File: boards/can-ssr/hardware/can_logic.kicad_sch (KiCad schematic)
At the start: 31 parts, among them J1 CAN IN, J2 CAN OUT, J3 ICSP, J4 UART, SW1 ADDR, U1 R-78E5.0-1.0, U2 MCP2562FD-E/P, U3 PIC18F47Q84-I/PT, Y1 16MHz

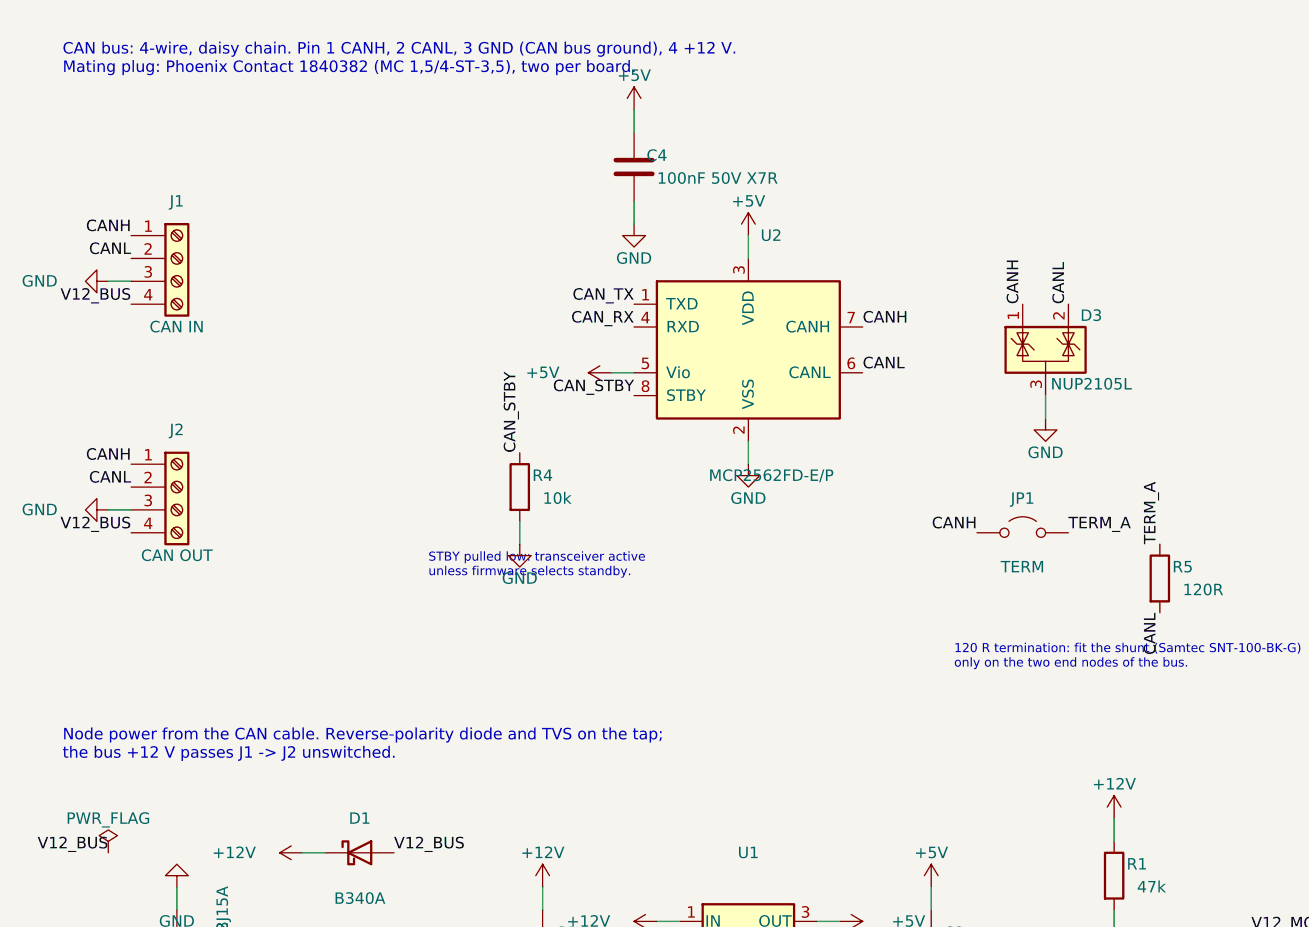
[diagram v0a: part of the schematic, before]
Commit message: can-ssr: stack interface rework; MCDN double-level CAN header; Ethernet parts
can-ssr (checker clean: ERC, DRC, schematic parity):
- M4 standoff holes 4.5 mm in from each corner (91 x 91 mm), new
  Thl_Mechanical:MountingHole_4.3mm_M4_Standoff7mm (4.3 mm courtyard, both
  sides); copper keep-outs around the load-side holes
- Load bolts moved inward (S+ 18, S- 36, L- 63, L+ 82 mm) with bars, mask
  openings, return bar, pours and labels
- Top-right corner reworked for the MH2 standoff (LED column, R50/C44,
  local reroutes); scoped DRC rule for MH2 beside U40
- CAN IN + CAN OUT -> one Phoenix MCDN 1,5/4-G1-3,5 P26 THR (1953732) at the
  stack CAN position (pin 1 at y 15.5 mm); schematic J1 is Conn_02x04,
  J2 removed; SW1/D2 moved; affected nets rejoined locally
- One-off rework scripts kept in hardware/stack_rework/

Library and tools:
- Footprint generator for the MCDN header (own drawing from Phoenix's
  dimensions); vendor STEP is local-only (SamacSys licence)
- tools/miniroute.py: small two-layer grid router for local rework

Requirements: stack CAN position fixed at pin 1 = 15.5 mm; holes at 4.5 mm;
can-controller Ethernet parts JD0-0004NL jack and HI1206P121R-10 bead (W6100).

Co-Authored-By: Claude Opus 5.5 <noreply@anthropic.com>
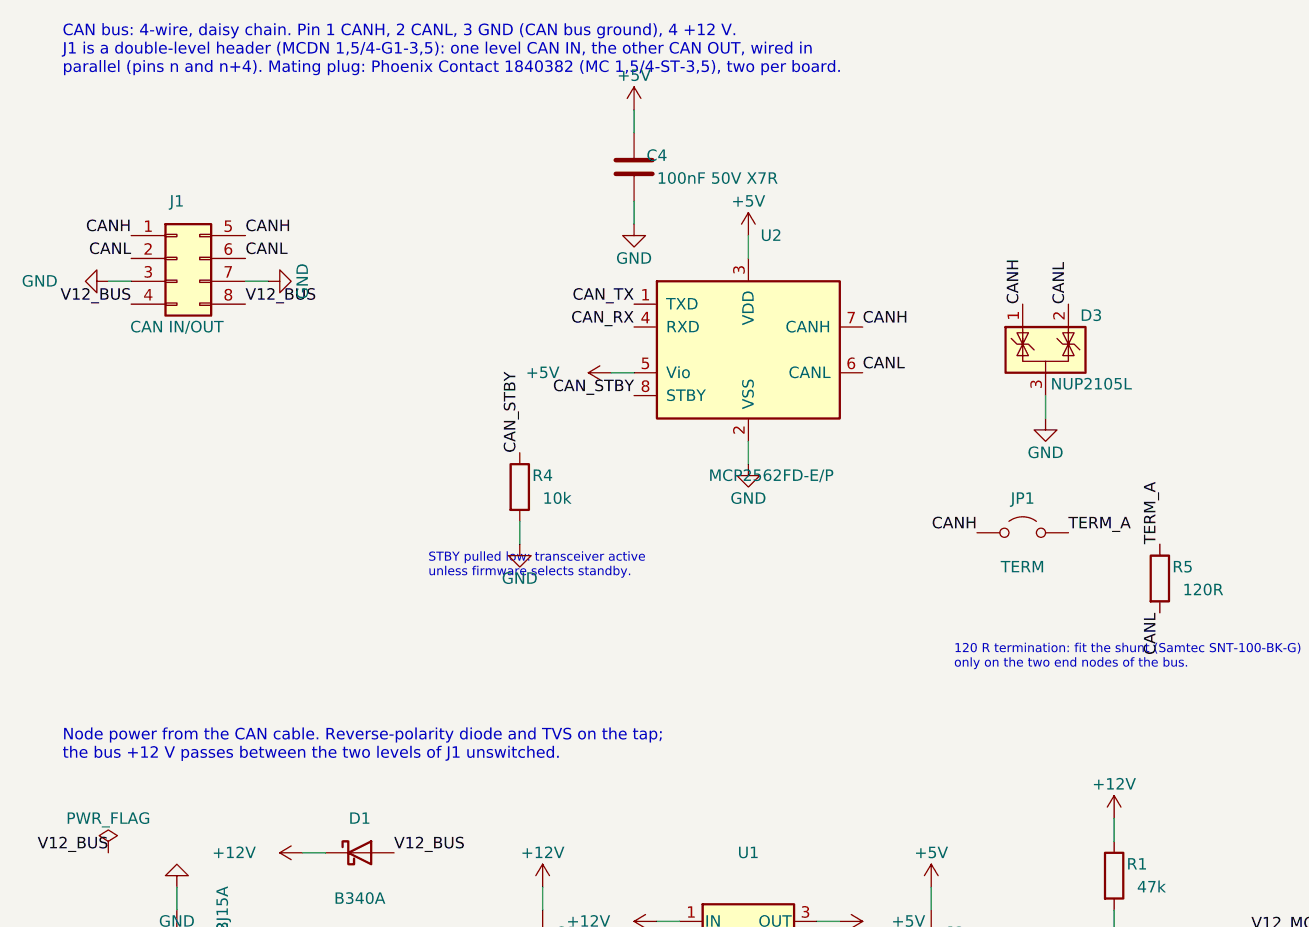
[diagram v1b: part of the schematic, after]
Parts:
- removed J2: CAN OUT, Connector_Phoenix_MC:PhoenixContact_MC_1,5_4-G-3.5_1x04_P3.50mm_Horizontal, symbol Connector:Screw_Terminal_01x04
- J1: value CAN IN -> CAN IN/OUT; footprint Connector_Phoenix_MC:PhoenixContact_MC_1,5_4-G-3.5_1x04_P3.50mm_Horizontal -> Thl_Connector:PhoenixContact_MCDN_1,5_4-G1-3,5_2x04_P3.5mm_Horizontal; symbol Connector:Screw_Terminal_01x04 -> Connector_Generic:Conn_02x04_Top_Bottom; MPN 1844236 -> 1953732
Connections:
- net CANH: now also J1.5 (Pin_5)
- net CANL: now also J1.6 (Pin_6)
- net GND: now also J1.7 (Pin_7)
- net V12_BUS: now also J1.8 (Pin_8)
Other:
- note added: "CAN bus: 4-wire, daisy chain. Pin 1 CANH, 2 CANL, 3 GND (CAN bus ground), 4 +12 V. J1 is a double-level header (MCDN 1,5/4-G1-3,5): one level CAN IN, the other CAN OUT, wired in parallel (pins n and n+4). Mating plug: Phoenix Contact 1840382 (MC 1,5/4-ST-3,5), two per board."
- note added: "Node power from the CAN cable. Reverse-polarity diode and TVS on the tap; the bus +12 V passes between the two levels of J1 unswitched."
- note removed: "CAN bus: 4-wire, daisy chain. Pin 1 CANH, 2 CANL, 3 GND (CAN bus ground), 4 +12 V. Mating plug: Phoenix Contact 1840382 (MC 1,5/4-ST-3,5), two per board."
- note removed: "Node power from the CAN cable. Reverse-polarity diode and TVS on the tap; the bus +12 V passes J1 -> J2 unswitched."
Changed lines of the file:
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@@
 		(rev "A")
 	)
-	(text "CAN bus: 4-wire, daisy chain. Pin 1 CANH, 2 CANL, 3 GND (CAN bus ground), 4 +12 V.\nMating plug: Phoenix Contact 1840382 (MC 1,5/4-ST-3,5), two per board."
+	(text "CAN bus: 4-wire, daisy chain. Pin 1 CANH, 2 CANL, 3 GND (CAN bus ground), 4 +12 V.\nJ1 is a double-level header (MCDN 1,5/4-G1-3,5): one level CAN IN, the other CAN OUT, wired in\nparallel (pins n and n+4). Mating plug: Phoenix Contact 1840382 (MC 1,5/4-ST-3,5), two per board."
 		(exclude_from_sim no)
 		(at 25.4 30.48 0)
@@
 	)
 	(symbol
-		(lib_id "Connector:Screw_Terminal_01x04")
+		(lib_id "Connector_Generic:Conn_02x04_Top_Bottom")
 		(at 38.1 50.8 0)
 		(unit 1)
@@
 			)
 		)
-		(property "Value" "CAN IN"
+		(property "Value" "CAN IN/OUT"
 			(at 38.1 58.42 0)
 			(effects
@@
 			)
 		)
-		(property "Footprint" "Connector_Phoenix_MC:PhoenixContact_MC_1,5_4-G-3.5_1x04_P3.50mm_Horizontal"
+		(property "Footprint" "Thl_Connector:PhoenixContact_MCDN_1,5_4-G1-3,5_2x04_P3.5mm_Horizontal"
 			(at 38.1 50.8 0)
 			(hide yes)
@@
 			)
 		)
-		(property "MPN" "1844236"
+		(property "MPN" "1953732"
 			(at 38.1 50.8 0)
 			(hide yes)
@@
 		)
 		(pin "4"
+		)
+		(pin "5"
+		)
+		(pin "6"
+		)
+		(pin "7"
+		)
+		(pin "8"
 		)
 		(instances
@@
 		)
 	)
-	(symbol
-		(lib_id "Connector:Screw_Terminal_01x04")
-		(at 38.1 76.2 0)
-		(unit 1)
-		(exclude_from_sim no)
-		(in_bom yes)
-		(on_board yes)
-		(dnp no)
-		(property "Reference" "J2"
-			(at 38.1 69.85 0)
-			(effects
-				(font
-					(size 1.27 1.27)
-				)
-			)
-		)
-		(property "Value" "CAN OUT"
-			(at 38.1 83.82 0)
-			(effects
-				(font
-					(size 1.27 1.27)
-				)
-			)
-		)
-		(property "Footprint" "Connector_Phoenix_MC:PhoenixContact_MC_1,5_4-G-3.5_1x04_P3.50mm_Horizontal"
-			(at 38.1 76.2 0)
-			(hide yes)
-			(effects
-				(font
-					(size 1.27 1.27)
-				)
-			)
-		)
-		(property "Datasheet" ""
-			(at 38.1 76.2 0)
-			(hide yes)
-			(effects
-				(font
-					(size 1.27 1.27)
-				)
-			)
-		)
-		(property "Description" ""
-			(at 38.1 76.2 0)
-			(hide yes)
-			(effects
-				(font
-					(size 1.27 1.27)
-				)
-			)
-		)
-		(property "Manufacturer" "Phoenix Contact"
-			(at 38.1 76.2 0)
-			(hide yes)
-			(effects
-				(font
-					(size 1.27 1.27)
-				)
-			)
-		)
-		(property "MPN" "1844236"
-			(at 38.1 76.2 0)
-			(hide yes)
-			(effects
-				(font
-					(size 1.27 1.27)
-				)
-			)
-		)
-		(pin "1"
-		)
-		(pin "2"
-		)
-		(pin "3"
-		)
-		(pin "4"
-		)
-		(instances
-			(project "can-ssr"
-				(path "/09b96810-cbdb-496a-83a0-e49ecf8d36fe/c853aef6-a14e-49c9-8f13-7d5eddc0f3e9"
-					(reference "J2")
-					(unit 1)
-				)
-			)
-		)
-	)
 	(label "CANH"
-		(at 33.02 73.66 180)
-		(effects
-			(font
-				(size 1.27 1.27)
-			)
-			(justify right bottom)
+		(at 45.72 48.26 0)
+		(effects
+			(font
+				(size 1.27 1.27)
+			)
+			(justify left bottom)
 		)
 	)
 	(label "CANL"
-		(at 33.02 76.2 180)
-		(effects
-			(font
-				(size 1.27 1.27)
-			)
-			(justify right bottom)
+		(at 45.72 50.8 0)
+		(effects
+			(font
+				(size 1.27 1.27)
+			)
+			(justify left bottom)
 		)
 	)
 	(wire
 		(pts
-			(xy 33.02 78.74) (xy 30.48 78.74)
+			(xy 45.72 53.34) (xy 48.26 53.34)
 		)
 		(stroke
@@
 	(symbol
 		(lib_id "power:GND")
-		(at 30.48 78.74 270)
+		(at 48.26 53.34 90)
 		(unit 1)
 		(exclude_from_sim no)
@@
 		(dnp no)
 		(property "Reference" "#PWR02"
-			(at 30.48 76.2 0)
+			(at 48.26 50.8 0)
 			(hide yes)
 			(effects
@@
 		)
 		(property "Value" "GND"
-			(at 22.86 78.74 270)
+			(at 52.07 53.34 0)
 			(effects
 				(font
@@
 		)
 		(property "Footprint" ""
-			(at 30.48 78.74 0)
-			(hide yes)
-			(effects
-				(font
-					(size 1.27 1.27)
-				)
-			)
-		)
-		(property "Datasheet" ""
-			(at 30.48 78.74 0)
-			(hide yes)
-			(effects
-				(font
-					(size 1.27 1.27)
-				)
-			)
-		)
-		(property "Description" ""
-			(at 30.48 78.74 0)
+			(at 48.26 53.34 0)
+			(hide yes)
+			(effects
+				(font
+					(size 1.27 1.27)
+				)
+			)
+		)
+		(property "Datasheet" ""
+			(at 48.26 53.34 0)
+			(hide yes)
+			(effects
+				(font
+					(size 1.27 1.27)
+				)
+			)
+		)
+		(property "Description" ""
+			(at 48.26 53.34 0)
 			(hide yes)
 			(effects
@@
 	)
 	(label "V12_BUS"
-		(at 33.02 81.28 180)
-		(effects
-			(font
-				(size 1.27 1.27)
-			)
-			(justify right bottom)
+		(at 45.72 55.88 0)
+		(effects
+			(font
+				(size 1.27 1.27)
+			)
+			(justify left bottom)
 		)
 	)
@@
 		)
 	)
-	(text "Node power from the CAN cable. Reverse-polarity diode and TVS on the tap;\nthe bus +12 V passes J1 -> J2 unswitched."
+	(text "Node power from the CAN cable. Reverse-polarity diode and TVS on the tap;\nthe bus +12 V passes between the two levels of J1 unswitched."
 		(exclude_from_sim no)
 		(at 25.4 106.68 0)

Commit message: Move core, can-card, io-card, serial-card, can-ssr, probe-helper to rev B
Rev A went to PCBWay and is tagged revA. Rev B replaces parts the Mouser
BOM check flagged (obsolete, end of life, not recommended for new designs,
or not orderable) and swaps out-of-stock passives and diodes for in-stock
equivalents. Field-only changes, same footprints, no layout change; the
reference boards (can-controller, pic-module) get the same part numbers.
The rev A order lists (DigiKey, Mouser) carry the same substitutions; the
Mouser list leaves out the T821 box headers (bought from DigiKey).

docs/rev-b-changes.md lists every change and the rev B to-dos (MAX7219 is
obsolete and must be replaced). transfer/mouser-revA.xlsx (Mouser BOM
check) consumed.

Co-Authored-By: Claude Opus 5.5 <noreply@anthropic.com>
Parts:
- C1, C2, C7: MPN GRM31CR71E106KA12L -> CL31B106KAHNNNE; Manufacturer Murata -> Samsung Electro-Mechanics
- C3, C4, C5, C6: MPN GRM21BR71H104KA01L -> C0805C104K5RACTU; Manufacturer Murata -> KEMET
- C8, C9: MPN GRM2165C1H270JA01D -> C0805C270J5GACTU; Manufacturer Murata -> KEMET
- D4: MPN LTST-C150GKT -> LTST-C150KGKT
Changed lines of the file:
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@@
 		(title "CAN SSR: CAN, power, MCU")
 		(date "2026-10-04")
-		(rev "A")
+		(rev "B")
 	)
 	(text "CAN bus: 4-wire, daisy chain. Pin 1 CANH, 2 CANL, 3 GND (CAN bus ground), 4 +12 V.\nJ1 is a double-level header (MCDN 1,5/4-G1-3,5): one level CAN IN, the other CAN OUT, wired in\nparallel (pins n and n+4). Mating plug: Phoenix Contact 1840382 (MC 1,5/4-ST-3,5), two per board."
@@
 			)
 		)
-		(property "Manufacturer" "Murata"
+		(property "Manufacturer" "KEMET"
 			(at 88.9 40.64 0)
 			(hide yes)
@@
 			)
 		)
-		(property "MPN" "GRM21BR71H104KA01L"
+		(property "MPN" "C0805C104K5RACTU"
 			(at 88.9 40.64 0)
 			(hide yes)
@@
 			)
 		)
-		(property "Manufacturer" "Murata"
+		(property "Manufacturer" "Samsung Electro-Mechanics"
 			(at 78.74 127 0)
 			(hide yes)
@@
 			)
 		)
-		(property "MPN" "GRM31CR71E106KA12L"
+		(property "MPN" "CL31B106KAHNNNE"
 			(at 78.74 127 0)
 			(hide yes)
@@
 			)
 		)
-		(property "Manufacturer" "Murata"
+		(property "Manufacturer" "Samsung Electro-Mechanics"
 			(at 121.92 127 0)
 			(hide yes)
@@
 			)
 		)
-		(property "MPN" "GRM31CR71E106KA12L"
+		(property "MPN" "CL31B106KAHNNNE"
 			(at 121.92 127 0)
 			(hide yes)
@@
 			)
 		)
-		(property "Manufacturer" "Murata"
+		(property "Manufacturer" "KEMET"
 			(at 157.48 132.08 0)
 			(hide yes)
@@
 			)
 		)
-		(property "MPN" "GRM21BR71H104KA01L"
+		(property "MPN" "C0805C104K5RACTU"
 			(at 157.48 132.08 0)
 			(hide yes)
@@
 			)
 		)
-		(property "Manufacturer" "Murata"
+		(property "Manufacturer" "KEMET"
 			(at 223.52 60.96 0)
 			(hide yes)
@@
 			)
 		)
-		(property "MPN" "GRM21BR71H104KA01L"
+		(property "MPN" "C0805C104K5RACTU"
 			(at 223.52 60.96 0)
 			(hide yes)
@@
 			)
 		)
-		(property "Manufacturer" "Murata"
+		(property "Manufacturer" "KEMET"
 			(at 246.38 60.96 0)
 			(hide yes)
@@
 			)
 		)
-		(property "MPN" "GRM21BR71H104KA01L"
+		(property "MPN" "C0805C104K5RACTU"
 			(at 246.38 60.96 0)
 			(hide yes)
@@
 			)
 		)
-		(property "Manufacturer" "Murata"
+		(property "Manufacturer" "Samsung Electro-Mechanics"
 			(at 269.24 60.96 0)
 			(hide yes)
@@
 			)
 		)
-		(property "MPN" "GRM31CR71E106KA12L"
+		(property "MPN" "CL31B106KAHNNNE"
 			(at 269.24 60.96 0)
 			(hide yes)
@@
 			)
 		)
-		(property "Manufacturer" "Murata"
+		(property "Manufacturer" "KEMET"
 			(at 187.96 60.96 0)
 			(hide yes)
@@
 			)
 		)
-		(property "MPN" "GRM2165C1H270JA01D"
+		(property "MPN" "C0805C270J5GACTU"
 			(at 187.96 60.96 0)
 			(hide yes)
@@
 			)
 		)
-		(property "Manufacturer" "Murata"
+		(property "Manufacturer" "KEMET"
 			(at 205.74 60.96 0)
 			(hide yes)
@@
 			)
 		)
-		(property "MPN" "GRM2165C1H270JA01D"
+		(property "MPN" "C0805C270J5GACTU"
 			(at 205.74 60.96 0)
 			(hide yes)
@@
 			)
 		)
-		(property "MPN" "LTST-C150GKT"
+		(property "MPN" "LTST-C150KGKT"
 			(at 241.3 180.34 0)
 			(hide yes)

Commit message: Rev B / rev A order: 10 uF CL31B106KAHZW6E, beads BLM31PG391SN1L
Both earlier substitutes (CL31B106KAHNNNE, BLM31KN102SH1L) are on
backorder at Mouser. CL31B106KAHZW6E has the same rating (1.4 mm tall).
The isolated-supply beads need no 1 kOhm: TI's reference uses 330 Ohm;
BLM31PG391SN1L is 390 Ohm @ 100 MHz, 2 A, 50 mOhm. Field-only changes;
order lists regenerated.

Co-Authored-By: Claude Opus 5.5 <noreply@anthropic.com>
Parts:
- C1, C2, C7: MPN CL31B106KAHNNNE -> CL31B106KAHZW6E
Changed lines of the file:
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@@
 			)
 		)
-		(property "MPN" "CL31B106KAHNNNE"
+		(property "MPN" "CL31B106KAHZW6E"
 			(at 78.74 127 0)
 			(hide yes)
@@
 			)
 		)
-		(property "MPN" "CL31B106KAHNNNE"
+		(property "MPN" "CL31B106KAHZW6E"
 			(at 121.92 127 0)
 			(hide yes)
@@
 			)
 		)
-		(property "MPN" "CL31B106KAHNNNE"
+		(property "MPN" "CL31B106KAHZW6E"
 			(at 269.24 60.96 0)
 			(hide yes)

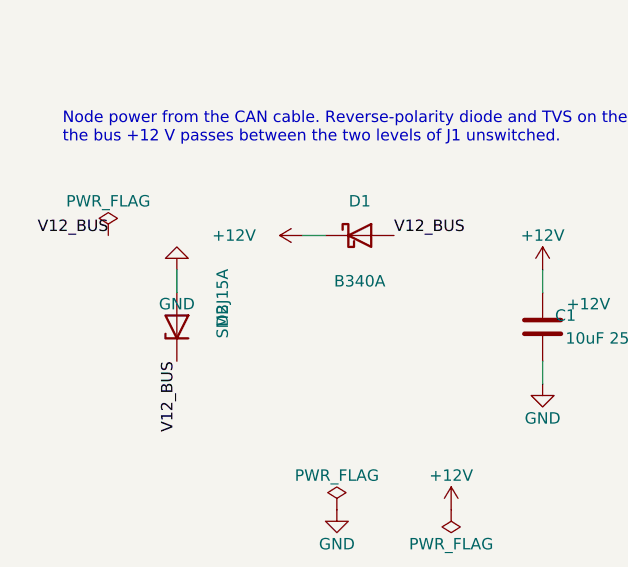
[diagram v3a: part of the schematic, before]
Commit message: Mouser cart: SQD50P04-09L P-FET, Diotec P6SMBJ15A TVS
Out of stock: Vishay SUD50P04-08-GE3 (core Q1) -> SQD50P04-09L_GE3 and
Littelfuse SMBJ15A (12 V input TVS) -> Diotec P6SMBJ15A, same footprints,
in core, can-ssr and the can-controller/pic-module references. Logged in
docs/rev-b-changes.md; order lists regenerated. The cart as ordered is
docs/orders/mouser-cart-2026-10-12.xls.

Co-Authored-By: Claude Opus 5.5 <noreply@anthropic.com>
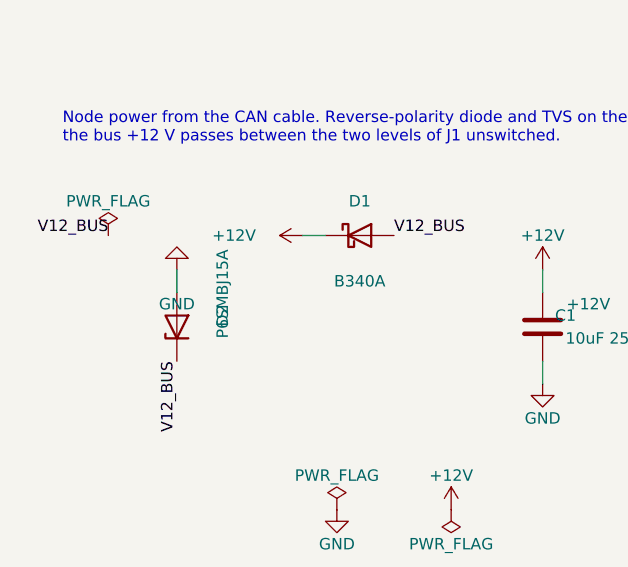
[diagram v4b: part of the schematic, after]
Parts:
- D2: value SMBJ15A -> P6SMBJ15A; MPN SMBJ15A -> P6SMBJ15A; Manufacturer Littelfuse -> Diotec Semiconductor
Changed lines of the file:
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@@
 			)
 		)
-		(property "Value" "SMBJ15A"
+		(property "Value" "P6SMBJ15A"
 			(at 43.18 128.27 0)
 			(effects
@@
 			)
 		)
-		(property "Manufacturer" "Littelfuse"
+		(property "Manufacturer" "Diotec Semiconductor"
 			(at 38.1 127 0)
 			(hide yes)
@@
 			)
 		)
-		(property "MPN" "SMBJ15A"
+		(property "MPN" "P6SMBJ15A"
 			(at 38.1 127 0)
 			(hide yes)
